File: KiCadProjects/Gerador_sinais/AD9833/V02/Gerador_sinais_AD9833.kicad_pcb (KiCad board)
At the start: 2 copper layers, 90 x 100 mm, 19 parts, among them J1 alimentacao analogica, J2 sinais analogicos, J3 comunicacao / sinais digitais, J4 Conn_01x07, U1 AD828AN, U2 X9c10x, U3 AD9833_module

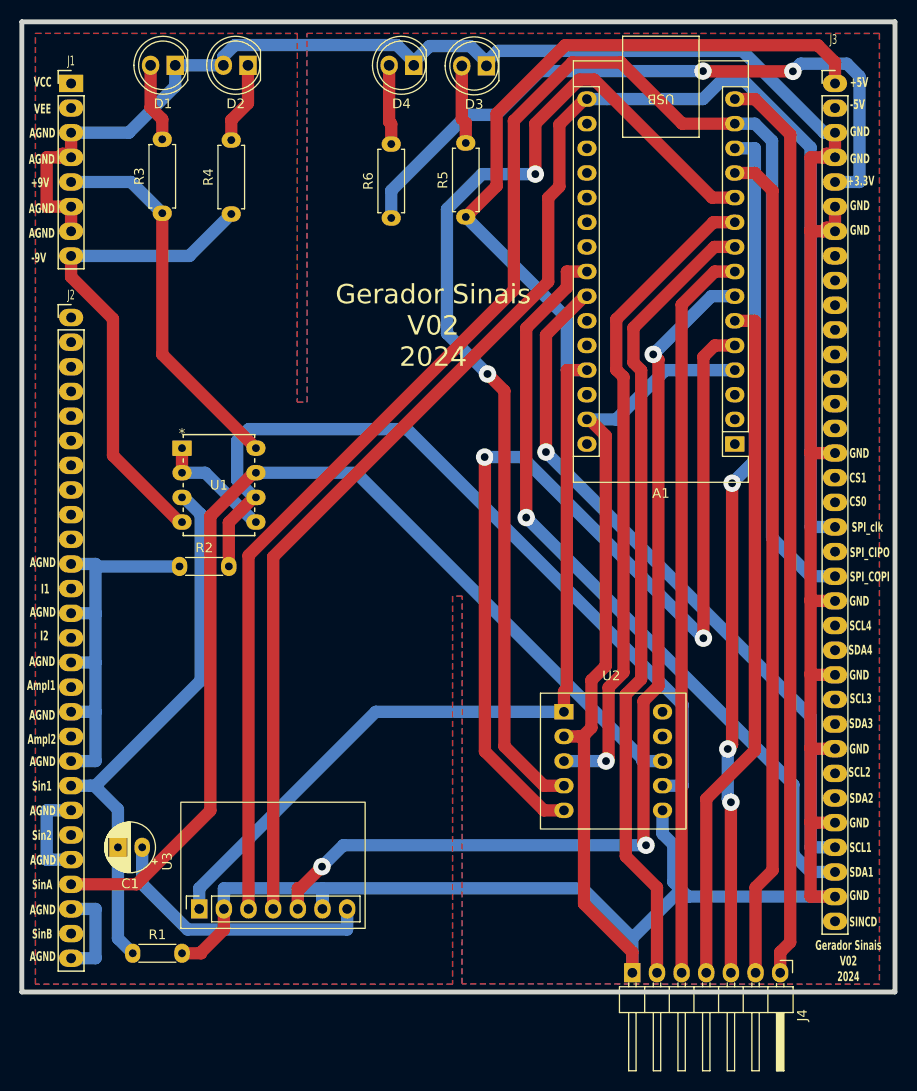
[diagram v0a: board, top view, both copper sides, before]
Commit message: mudança AmpOp n inversor
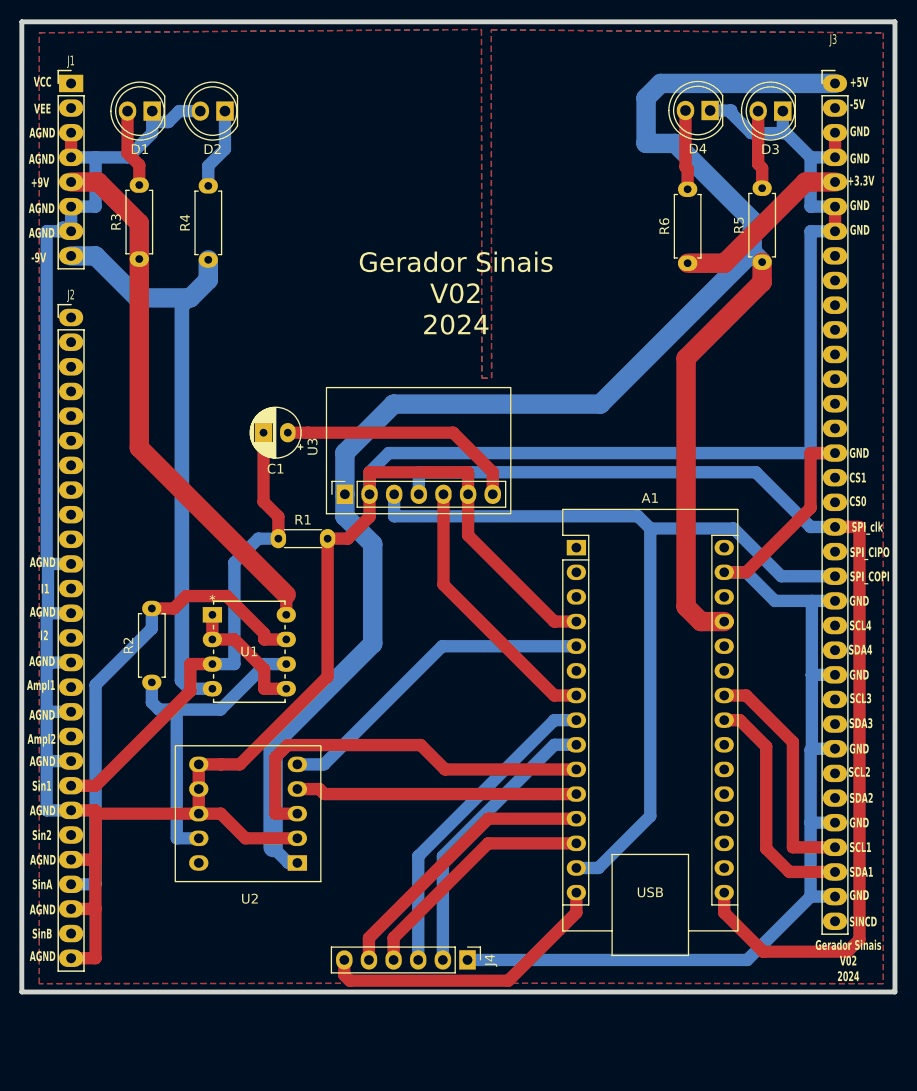
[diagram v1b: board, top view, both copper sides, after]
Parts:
- J4: value Conn_01x07 -> Conn_01x06; footprint Connector_PinHeader_2.54mm:PinHeader_1x07_P2.54mm_Horizontal -> Connector_PinHeader_2.54mm:PinHeader_1x06_P2.54mm_Vertical
- R2: value 2,7k -> 10k; footprint Resistor_THT:R_Axial_DIN0204_L3.6mm_D1.6mm_P5.08mm_Horizontal -> Resistor_THT:R_Axial_DIN0207_L6.3mm_D2.5mm_P7.62mm_Horizontal
- R3: value 390 -> 1.2k
- R4: value 360 -> 1.2k
- R5: value 160 -> 390
- R6: value 82 -> 240
- moved R1 45.3 mm to (128.0, 104.1)
- moved U3 45.3 mm to (134.9, 99.5)
- moved C1 45.3 mm to (129.0, 93.2)
- moved U2 38.0 mm to (124.9, 132.4), turned to 180 degrees
- moved J4 32.3 mm to (147.5, 147.5)
- moved D4 30.9 mm to (172.6, 59.9)
- moved D3 30.9 mm to (180.0, 60.0)
- moved R5 30.9 mm to (177.9, 75.6)
- moved R6 30.9 mm to (170.2, 75.7)
- moved A1 19.5 mm to (158.8, 105.0), turned to 0 degrees
- moved U1 17.5 mm to (121.2, 111.9)
- moved R2 12.3 mm to (115.0, 118.9), turned to 90 degrees
- moved R3 5.28 mm to (113.7, 75.2)
- moved R4 5.28 mm to (120.8, 75.3)
- moved D1 5.28 mm to (115.0, 60.0)
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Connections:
- A1 pad 6: storage_R -> unconnected-(A1-D3-Pad6)
- A1 pad 8: Up_pot -> Up_gain
- A1 pad 9: Down_pot -> Down_gain
- J4 pad 1: S_wave -> Earth
- J4 pad 2: freq+ -> Down_gain
- J4 pad 3: freq- -> Up_gain
- J4 pad 4: storage_R -> freq-
- J4 pad 5: Up_pot -> freq+
- J4 pad 6: Down_pot -> S_wave
- R2 pad 1: Earth -> Net-(U1--IN2)
- R2 pad 2: Net-(U1--IN2) -> Out_circuito
- U2 pad 7: Net-(U1--IN2) -> Earth
- U2 pad 8: Out_circuito -> Earth
- U2 pad 9: unconnected-(U2-RH-Pad9) -> Net-(U1--IN2)
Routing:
- net SPI_COPI: track 174.1 -> 89.8 mm
- net Down_pot: track 82.7 -> 0.00 mm
- net X9c10x_U/D: track 108.9 -> 29.0 mm, vias 2 -> 0
- net Up_pot: track 75.8 -> 0.00 mm
- net CS (AD9833): track 102.3 -> 27.7 mm, vias 3 -> 0
- net storage_R: track 71.3 -> 0.00 mm
- net CS (X9c104): track 104.0 -> 33.8 mm, vias 2 -> 0
- net S_wave: track 94.1 -> 30.7 mm
- net freq-: track 88.3 -> 25.1 mm, vias 3 -> 0
- net Out_circuito: track 108.7 -> 49.9 mm
- net freq+: track 86.0 -> 28.7 mm
- net SDA1: track 80.4 -> 24.1 mm, vias 1 -> 0
- net SPI_clk: track 165.4 -> 110.7 mm
- net +3.3V: track 70.5 -> 18.7 mm, vias 2 -> 0
- net Net-(U1--IN2): track 83.7 -> 33.8 mm
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
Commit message: Baseado barramento v04 - Finalizado - implementacao resistor pullup i2c 2
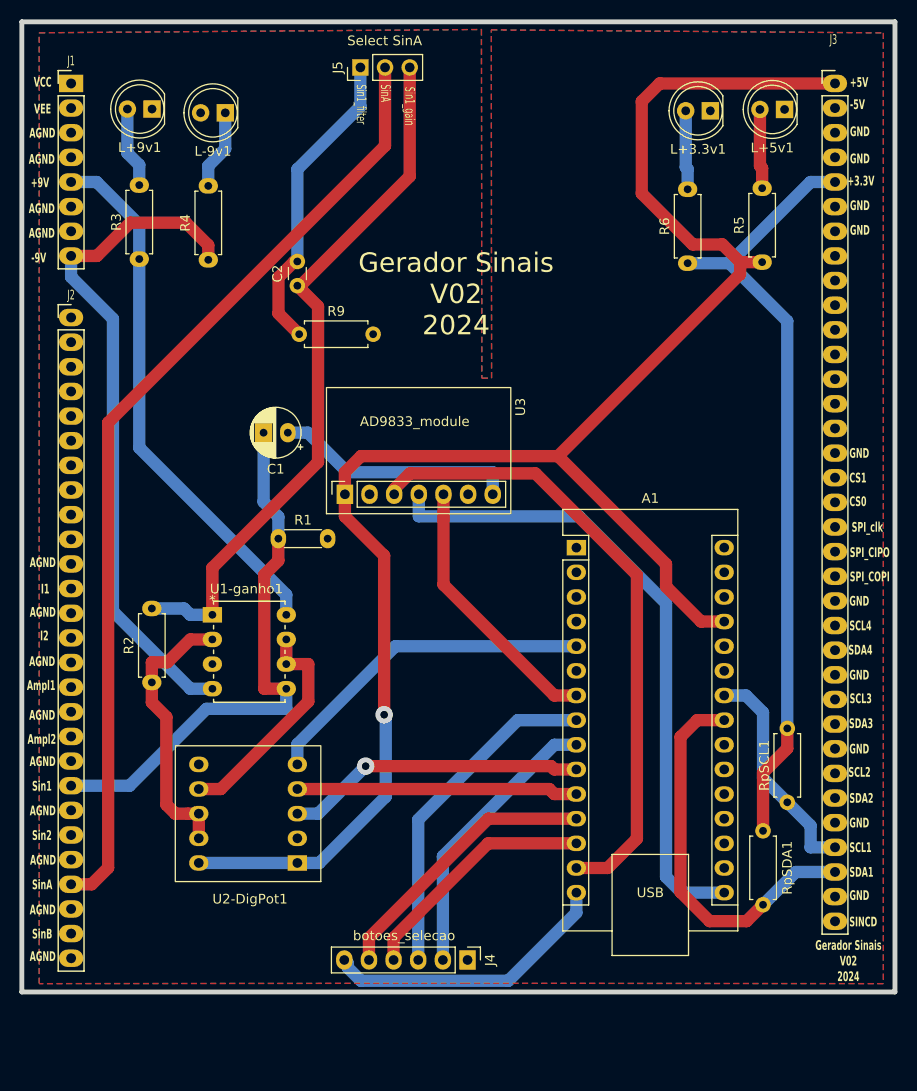
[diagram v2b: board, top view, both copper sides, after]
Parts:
- removed D1: LED - Blue, LED_THT:LED_D5.0mm
- removed D2: LED - Red, LED_THT:LED_D5.0mm
- removed D3: LED - Green, LED_THT:LED_D5.0mm
- removed D4: LED - Yelow, LED_THT:LED_D5.0mm
- added C2: 100nF, Capacitor_THT:C_Disc_D3.0mm_W1.6mm_P2.50mm, F.Cu at (130.0, 78.0)
- added J5: Select SinA, Connector_PinHeader_2.54mm:PinHeader_1x03_P2.54mm_Vertical, F.Cu at (136.5, 55.5)
- added L+3.3v1: LED - Yelow, LED_THT:LED_D5.0mm, F.Cu at (172.6, 60.0)
- added L+5v1: LED Green, LED_THT:LED_D5.0mm, F.Cu at (180.2, 59.8)
- added L+9v1: LED Blue, LED_THT:LED_D5.0mm, F.Cu at (115.0, 59.8)
- added L-9v1: LED Red, LED_THT:LED_D5.0mm, F.Cu at (122.6, 60.2)
- added R9: 160k, Resistor_THT:R_Axial_DIN0207_L6.3mm_D2.5mm_P7.62mm_Horizontal, F.Cu at (130.2, 83.0)
- added RpSCL1: 4k7, Resistor_THT:R_Axial_DIN0207_L6.3mm_D2.5mm_P7.62mm_Horizontal, F.Cu at (180.5, 131.2)
- added RpSDA1: 4k7, Resistor_THT:R_Axial_DIN0207_L6.3mm_D2.5mm_P7.62mm_Horizontal, F.Cu at (178.0, 141.8)
- J4: value Conn_01x06 -> botoes_selecao
- R1: value 10k -> 160k
- renumbered U1 to U1-ganho1, U2 to U2-DigPot1
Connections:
- A1 pad 14: SPI_COPI -> SPI_COPI  (AD9833)
- A1 pad 16: SPI_clk -> SPI_clk  (AD9833)
- C1 pad 2: Passa_alta -> Sin1
- J2 pad 20: Passa_alta -> Sin1
- J2 pad 24: Out_circuito -> SinA
- R1 pad 1: Passa_alta -> Sin1
- R2 pad 1: Net-(U1--IN2) -> Net-(U1-ganho1--IN1)
- R2 pad 2: Out_circuito -> Sin1_gain
- U1-ganho1 pad 1: out_buffer -> Sin1_gain
- U1-ganho1 pad 2: out_buffer -> Net-(U1-ganho1--IN1)
- U1-ganho1 pad 3: Passa_alta -> Earth
- U1-ganho1 pad 5: out_buffer -> Sin1
- U1-ganho1 pad 6: Net-(U1--IN2) -> OutBuffer
- U1-ganho1 pad 7: Out_circuito -> OutBuffer
- U2-DigPot1 pad 10: unconnected-(U2-VCC-Pad10) -> +5V
- U2-DigPot1 pad 7: Earth -> OutBuffer
- U2-DigPot1 pad 8: Earth -> Net-(U1-ganho1--IN1)
- U2-DigPot1 pad 9: Net-(U1--IN2) -> Net-(U1-ganho1--IN1)
- U3 pad 3: SPI_COPI -> SPI_COPI  (AD9833)
- U3 pad 4: SPI_clk -> SPI_clk  (AD9833)
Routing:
- net Earth: track 450.4 -> 0.00 mm
- net SPI_clk: track 110.7 -> 0.00 mm
- net SinA: track 0.00 -> 98.8 mm
- net SPI_COPI: track 89.8 -> 0.00 mm
- net Sin1_gain: track 0.00 -> 73.2 mm
- net SPI_clk  (AD9833): track 0.00 -> 66.3 mm
- net SPI_COPI  (AD9833): track 0.00 -> 65.2 mm
- net +3.3V: track 18.7 -> 80.7 mm
- net Sin1: track 0.00 -> 57.4 mm
- net Passa_alta: track 51.2 -> 0.00 mm
- net Out_circuito: track 49.9 -> 0.00 mm
- net Net-(U1--IN2): track 33.8 -> 0.00 mm
- net Sin1_filter: track 0.00 -> 32.1 mm
- net Net-(U1-ganho1--IN1): track 0.00 -> 28.3 mm
- net OutBuffer: track 0.00 -> 23.7 mm
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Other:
- board text added: "Sin1_filter"
- board text added: "Sin1_gain"

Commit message: temp
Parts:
- removed RpSCL1, RpSDA1: 4k7, Resistor_THT:R_Axial_DIN0207_L6.3mm_D2.5mm_P7.62mm_Horizontal
- added J6: Encoder KY-040, Connector_PinHeader_2.54mm:PinHeader_1x05_P2.54mm_Vertical, F.Cu at (125.2, 147.3)
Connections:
- net S_wave renamed En3
- net freq+ renamed En2
- net freq- renamed En1
- A1 pad 23: SDA1 -> unconnected-(A1-A4-Pad23)
- A1 pad 24: SCL1 -> unconnected-(A1-A5-Pad24)
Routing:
- net +3.3V: track 80.7 -> 18.7 mm
- net SDA1: track 40.5 -> 0.00 mm
- net SCL1: track 23.2 -> 0.00 mm
- net En3: track 30.0 -> 48.5 mm
- net En1: track 25.1 -> 42.4 mm
- net En2: track 28.7 -> 45.2 mm
- net +5V: track 178.8 -> 189.5 mm
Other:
- board text added: "Gerador Sinais AD9833 - V02 2024"
- board text added: "Gerador Sinais AD9833 V02 2024"
- board text removed: "Gerador Sinais V02 2024"
